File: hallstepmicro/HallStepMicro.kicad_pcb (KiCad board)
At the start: 2 copper layers, 25.4 x 55.9 mm, 26 parts, among them IC1 ATTINY84A-SS

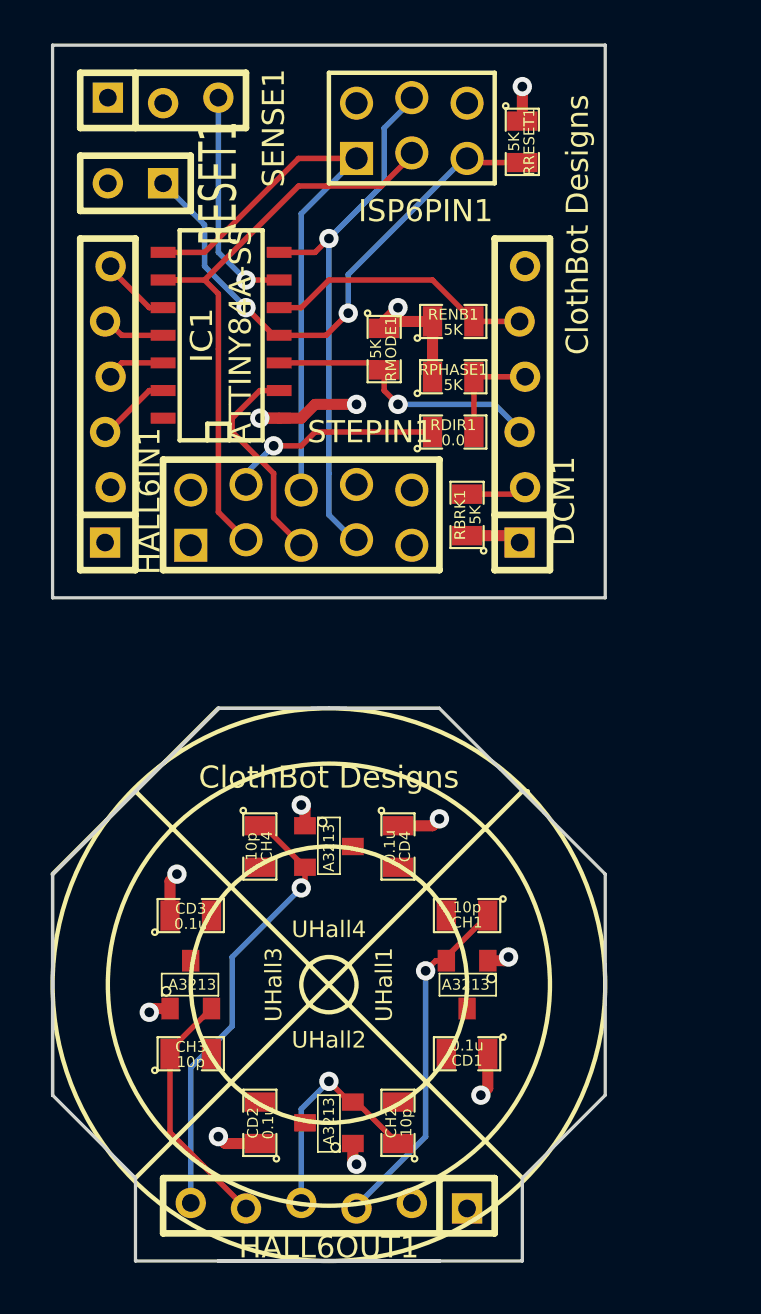
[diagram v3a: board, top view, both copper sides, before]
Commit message: Refined wiring in micro zone.
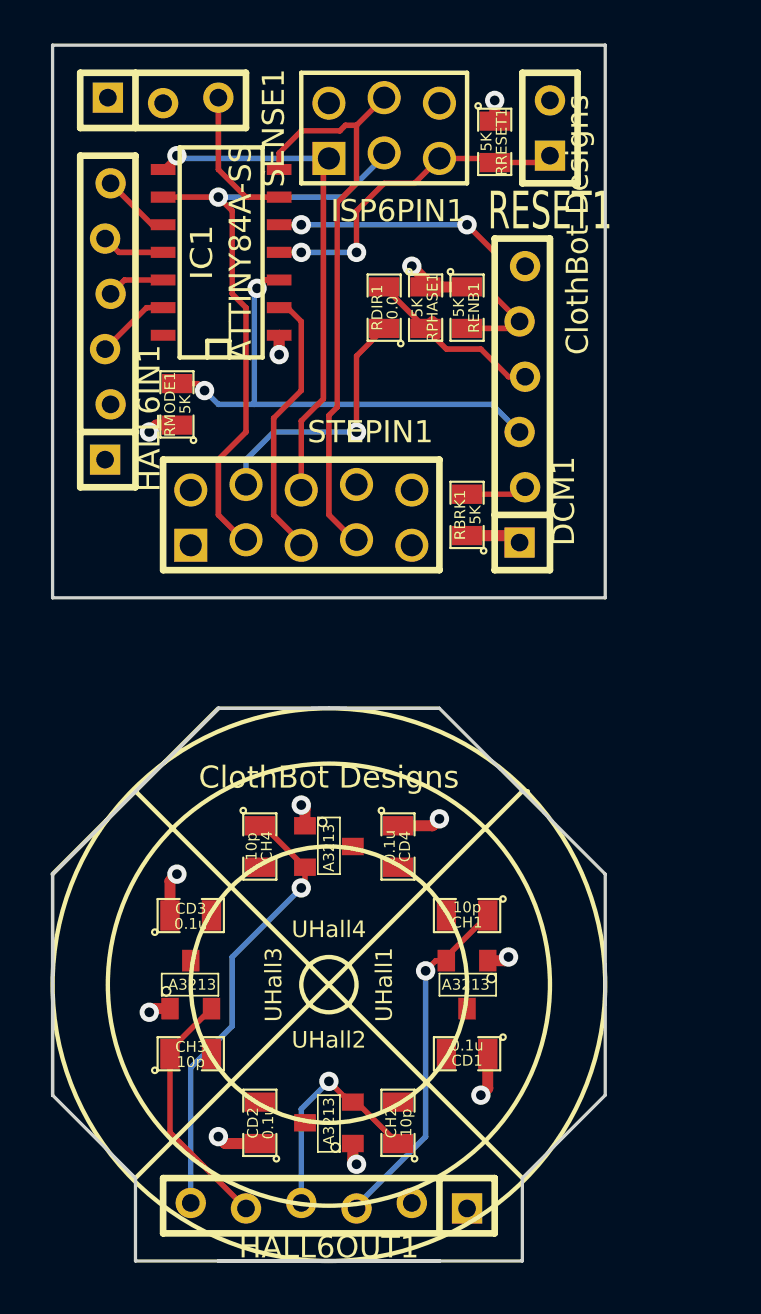
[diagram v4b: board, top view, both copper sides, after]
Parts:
- moved RESET1 19.2 mm to (137.2, 36.8), turned to 90 degrees
- moved RMODE1 9.86 mm to (120.0, 49.5), turned to 90 degrees
- moved RDIR1 6.54 mm to (129.5, 45.1), turned to 90 degrees
- moved HALL6IN1 3.81 mm to (116.8, 45.7)
- moved IC1 3.81 mm to (121.9, 42.5)
- moved RPHASE1 3.42 mm to (131.4, 45.1), turned to 270 degrees
- moved ISP6PIN1 1.27 mm to (129.5, 36.8)
- moved RRESET1 1.27 mm to (134.6, 37.5)
- moved RENB1 0.90 mm to (133.3, 45.1), turned to 270 degrees
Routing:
- net /DC_MODE: track 13.0 -> 23.2 mm, vias 1 -> 2
- net /RESET: track 25.1 -> 15.6 mm
- net VDD: track 15.1 -> 9.04 mm
- net /DC_ENABLE: track 12.5 -> 16.6 mm, vias 0 -> 2
- net /DC_PHASE: track 4.76 -> 8.50 mm
- net /SENSE: track 10.3 -> 6.62 mm, vias 1 -> 0
- net /STP_MIN: track 27.0 -> 23.7 mm, vias 0 -> 1
- net /STP_ENB: track 9.84 -> 12.6 mm
- net /STP_DIR: track 9.87 -> 12.0 mm
- net /STP_MAX: track 25.0 -> 26.8 mm, vias 1 -> 0
- net /STP_STEP: track 27.2 -> 28.5 mm, vias 0 -> 1

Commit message: Tweaking layout routing.
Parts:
- moved RMODE1 13.4 mm to (133.3, 48.9), turned to 270 degrees
- turned CH1 to 0 degrees
- turned CH2 to 270 degrees
- turned CH3 to 180 degrees
- turned CH4 to 90 degrees
- turned RENB1 to 90 degrees
- turned RRESET1 to 90 degrees
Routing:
- net VCC: track 12.2 -> 21.4 mm, vias 8 -> 4
- net /HallSensors1/hall2: track 10.5 -> 2.08 mm, vias 1 -> 0
- net /DC_MODE: track 23.2 -> 16.2 mm
- net /DC_ENABLE: track 16.6 -> 12.8 mm
- net /HallSensors1/hall3: track 11.4 -> 13.6 mm, vias 0 -> 1
- net VDD: track 9.04 -> 11.0 mm
- net /RESET: track 15.6 -> 16.7 mm
- net /HallSensors1/hall1: track 16.2 -> 15.2 mm
- net /STP_STEP: track 28.5 -> 27.4 mm
- net /HallSensors1/hall4: track 20.8 -> 20.0 mm
- net /STP_DIR: track 12.0 -> 11.4 mm
- net /STP_ENB: track 12.6 -> 13.1 mm
- net /DC_PHASE: track 8.50 -> 8.74 mm, vias 0 -> 1

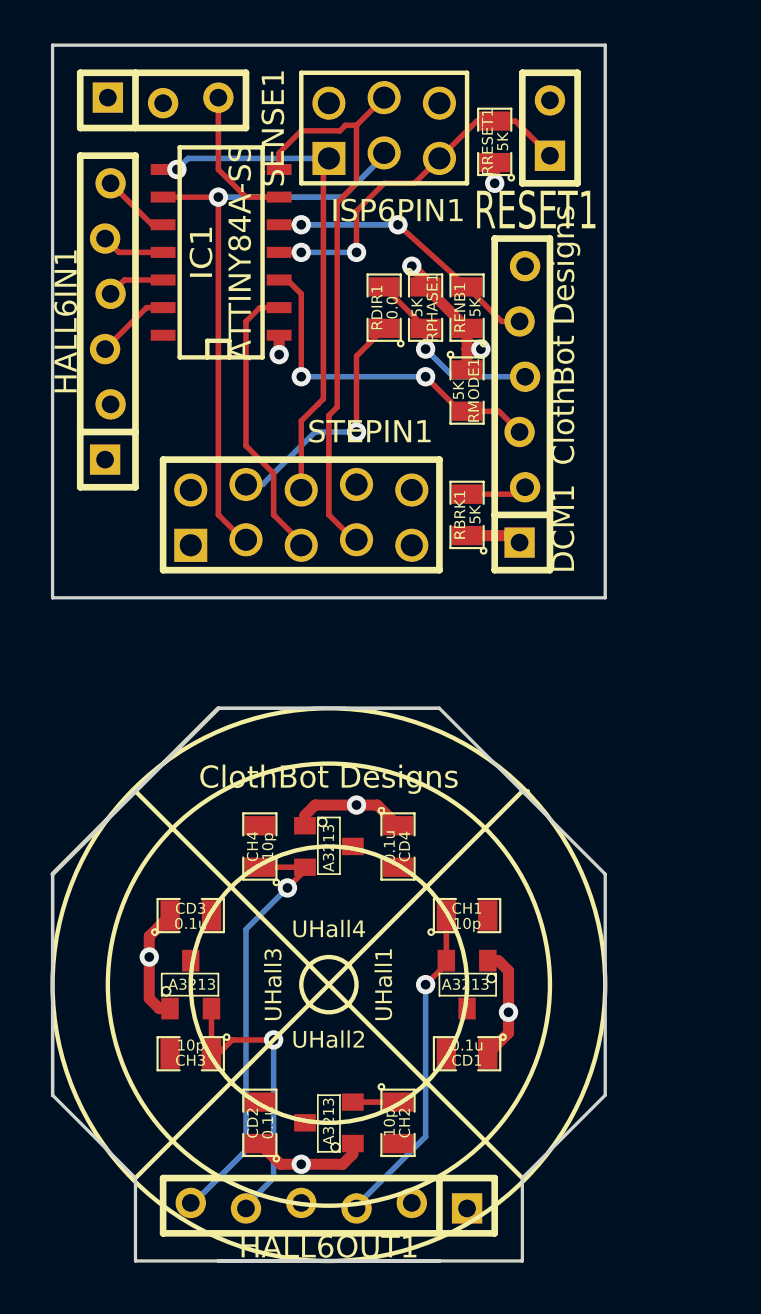
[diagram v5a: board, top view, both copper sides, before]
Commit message: Added optional pullup resistors to sensor board.
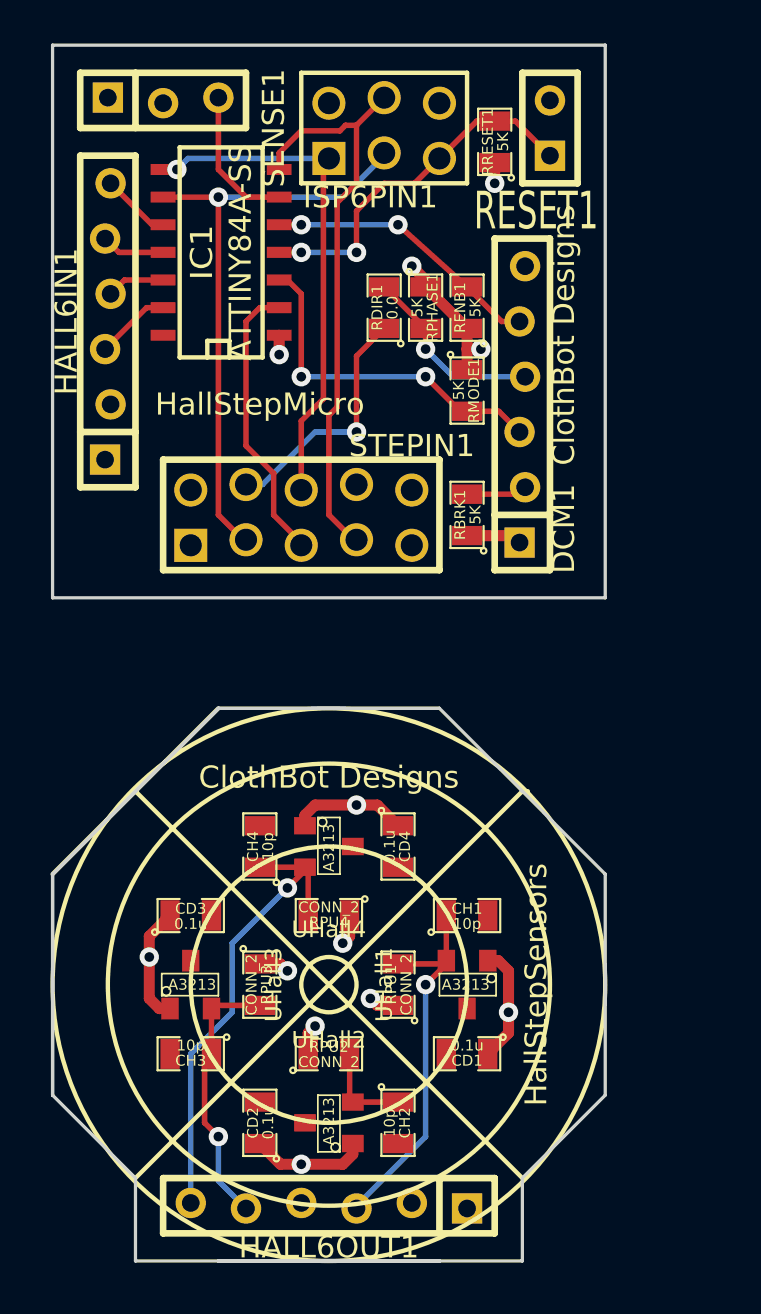
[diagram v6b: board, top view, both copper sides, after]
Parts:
- added RPU1: CONN_2, SM0805, F.Cu at (130.2, 76.2)
- added RPU2: CONN_2, SM0805, F.Cu at (127.0, 79.4)
- added RPU3: CONN_2, SM0805, F.Cu at (123.8, 76.2)
- added RPU4: CONN_2, SM0805, F.Cu at (127.0, 73.0)
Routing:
- net VCC: track 21.4 -> 27.0 mm, vias 4 -> 8
- net /HallSensors1/hall1: track 15.2 -> 17.5 mm
- net /HallSensors1/hall2: track 2.08 -> 4.36 mm
- net /HallSensors1/hall4: track 20.0 -> 22.2 mm
- net /HallSensors1/hall3: track 13.6 -> 12.5 mm
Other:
- board text added: "HallStepMicro"
- board text added: "HallStepSensors"
